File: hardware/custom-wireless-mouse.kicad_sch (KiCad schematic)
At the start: 31 parts, among them J1 SWD_HEADER, SW1 JS202011SCQN, SW2 EVQ-P7B01P, SW3 EVQ-P7B01P, SW4 EVQ-P7B01P, U1 nRF52810-QCAA-T, U2 PMW3610DM-SUDU, U3 TLV61220DBVT, Y1 NX2016SA-32MHZ

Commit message: Manual schematic cleanup pass (layout, routing, net naming)
Reworked wire routing and component placement by hand for readability,
and renamed several nets (VBAT/VBAT_SW, nRESET, etc). Known issues from
an audit of this pass, not yet fixed:

- J1's physical pin assignment no longer matches its own symbol's pin
  labels: pin 1 (labeled SWDIO) now carries nRESET, pin 3 (labeled GND)
  carries SWDIO, pin 4 (labeled ~RESET) carries GND. Only pin 2 (SWDCLK)
  is still correct.
- 5 of the 6 PWR_FLAG markers were removed, so ERC now flags U2's
  charge-pump/laser-driver nets, U3's VBAT net, and the GND net as
  undriven. Wiring on all of these is still correct per the netlist;
  this is only a missing ERC marker, not a wrong connection.
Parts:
- B1: value 1x AA (reused from kit) -> 1x AA
- C14: value 100nF X7R -> 100nF
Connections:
- net +VSYS: now also C1.1, C10.1, C11.1, C16.1, C2.1, C3.1, C4.1, C5.1, C8.1, C9.1, U1.1 (DEC1), U1.21 (DEC2), U1.22 (DEC3), U1.30 (DEC4); no longer C10.2, C11.2, C16.2, C5.2, C8.2, C9.2, L1.1, L1.2, U3.1 (SW)
- net GND: now also C1.2, C10.2, C11.2, C12.2, C13.2, C15.2, C16.2, C2.2, C3.2, C4.2, C5.2, C8.2, C9.2, J1.4 (~RESET); no longer C1.1, C10.1, C11.1, C12.1, C13.1, C15.1, C16.1, C2.1, C3.1, C4.1, C5.1, C8.1, C9.1, J1.3 (GND)
- net SWDIO: now reaches U1.18 (SWDIO)
- net SWDIO: now also J1.3 (GND); no longer J1.1 (SWDIO)
- net SWDCLK: now reaches J1.2 (SWDCLK), U1.17 (SWDCLK)
- net nRESET: now reaches U1.16 (P0.21/~{RESET})
- net nRESET: now also J1.1 (SWDIO); no longer J1.4 (~RESET)
- net VBAT_SW: now reaches SW1.1 (1A), U3.3 (EN), U3.6 (VBAT)
- net VBAT_SW: now also C15.1, L1.1; no longer B1.1 (+), C15.2, SW1.2 (2A)
- net at C6.2, U1.23 (XC1), Y1.3: no longer C7.1, U1.24 (XC2), Y1.1
- new net: B1.1 (+), SW1.2 (2A)
- new net: C12.1, C13.1, U2.9 (VCP)
- new net: U2.15 (XYLASER), U2.16 (-VCSEL)
- new net: L1.2, U3.1 (SW)
- new net: C7.1, U1.24 (XC2), Y1.1
- no-connect marks 7 -> 10
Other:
- note added: "MCU - U1 (nRF52810)"
- note removed: "MCU — U1 (nRF52810)"
- moved on the sheet: B1, C1, C10, C11, C12, C13, C15, C16, C2, C3, C4, C5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

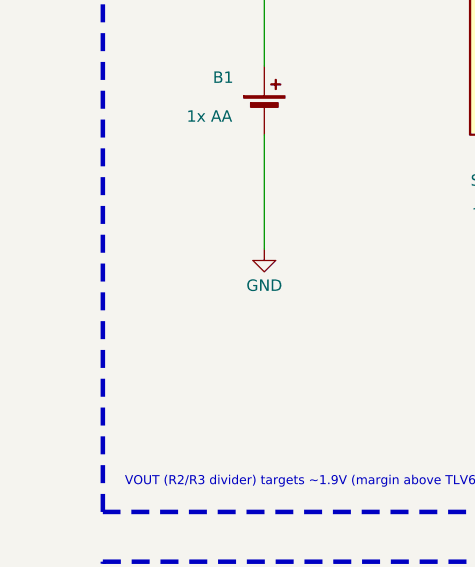
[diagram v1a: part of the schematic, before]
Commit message: Add JST B2B-XH-A battery connector to schematic and libraries
B1 (Device:Battery_Cell) is netted in the schematic but has an empty
Footprint field, so nothing would be placed on the PCB for it - there
was no physical way to actually plug in a battery. Added the JST XH
2-position pin header (B2B-XH-A) as J2, vendored from KiCad's own
official Connector_JST library (symbol, footprint, and 3D model, all
CC-BY-SA 4.0) plus its public datasheet. Placed unwired on the
schematic for manual wiring.
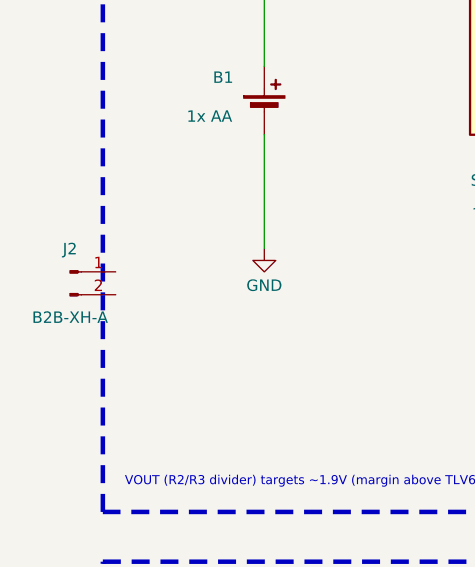
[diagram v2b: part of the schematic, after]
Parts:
- added J2: B2B-XH-A, jst-b2b-xh-a:battery-conn-jst-b2b-xh-a, symbol jst-b2b-xh-a:B2B-XH-A
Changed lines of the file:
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@@
+	)
+	(symbol
+		(lib_id "jst-b2b-xh-a:B2B-XH-A")
+		(at 12.7 90.17 0)
+		(unit 1)
+		(body_style 1)
+		(exclude_from_sim no)
+		(in_bom yes)
+		(on_board yes)
+		(in_pos_files yes)
+		(dnp no)
+		(property "Reference" "J2"
+			(at 12.7 87.63 0)
+			(show_name no)
+			(do_not_autoplace no)
+			(effects
+				(font
+					(size 1.27 1.27)
+				)
+			)
+		)
+		(property "Value" "B2B-XH-A"
+			(at 12.7 95.25 0)
+			(show_name no)
+			(do_not_autoplace no)
+			(effects
+				(font
+					(size 1.27 1.27)
+				)
+			)
+		)
+		(property "Footprint" "jst-b2b-xh-a:battery-conn-jst-b2b-xh-a"
+			(at 12.7 90.17 0)
+			(hide yes)
+			(show_name no)
+			(do_not_autoplace no)
+			(effects
+				(font
+					(size 1.27 1.27)
+				)
+			)
+		)
+		(property "Datasheet" "${KIPRJMOD}/datasheets/jst-xh-connector-series.pdf"
+			(at 12.7 90.17 0)
+			(hide yes)
+			(show_name no)
+			(do_not_autoplace no)
+			(effects
+				(font
+					(size 1.27 1.27)
+				)
+			)
+		)
+		(property "Description" "JST XH series 2.50mm-pitch battery connector, through-hole vertical pin header (mates with JST XHP-2 wire housing)"
+			(at 12.7 90.17 0)
+			(hide yes)
+			(show_name no)
+			(do_not_autoplace no)
+			(effects
+				(font
+					(size 1.27 1.27)
+				)
+			)
+		)
+		(pin "1"
+		)
+		(pin "2"
+		)
+		(instances
+			(project "custom-wireless-mouse"
+				(path "/d776ca83-3842-4947-ae63-5f40f232181f"
+					(reference "J2")
+					(unit 1)
+				)
+			)
+		)
 	)
 	(symbol

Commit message: Add reverse-battery and short-circuit protection parts (unwired)
Placed Q1 (Diodes Inc DMP2035U, low-threshold P-channel MOSFET) and F1
(Littelfuse 0603L010 PPTC resettable fuse) on the schematic near J2,
vendored with real datasheets. Q1 is a high-side ideal-diode reverse-
polarity protector (Source toward the battery, Drain toward the rest
of the circuit, Gate to GND); F1 is a self-resetting fuse sized well
above the design's peak draw but well below a battery short. Both
parts are placed only - not wired in - per request.

Also includes the removal of the old placeholder B1 (Device:Battery_Cell)
and repositioning of J2, done directly in the KiCad GUI.
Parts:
- removed B1: 1x AA, symbol Device:Battery_Cell
- added F1: 0603L010, littelfuse-0603l010:fuse-0603-littelfuse-0603l010, symbol littelfuse-0603l010:0603L010
- added Q1: DMP2035U, diodes-dmp2035u:sot-23-dmp2035u, symbol diodes-dmp2035u:DMP2035U
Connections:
- net GND: now also J2.2 (-)
- net at SW1.2 (2A): now also J2.1 (+)
- net FB: now reaches R2.2, R3.1, U3.4 (FB)
- net SW: now reaches L1.2, U3.1 (SW)
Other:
- note added: "MCU : U1 (nRF52810)"
- note added: "OPTICAL SENSOR : U2 (PMW3610)"
- note added: "POWER SUPPLY : U3 (TLV61220)"
- note added: "USER INPUT : WHEEL & BUTTONS"
- note removed: "MCU - U1 (nRF52810)"
- note removed: "OPTICAL SENSOR — U2 (PMW3610)"
- note removed: "POWER SUPPLY"
- note removed: "USER INPUT — WHEEL & BUTTONS"
- company: (none) -> Limp Dawg Customs
- moved on the sheet: J2

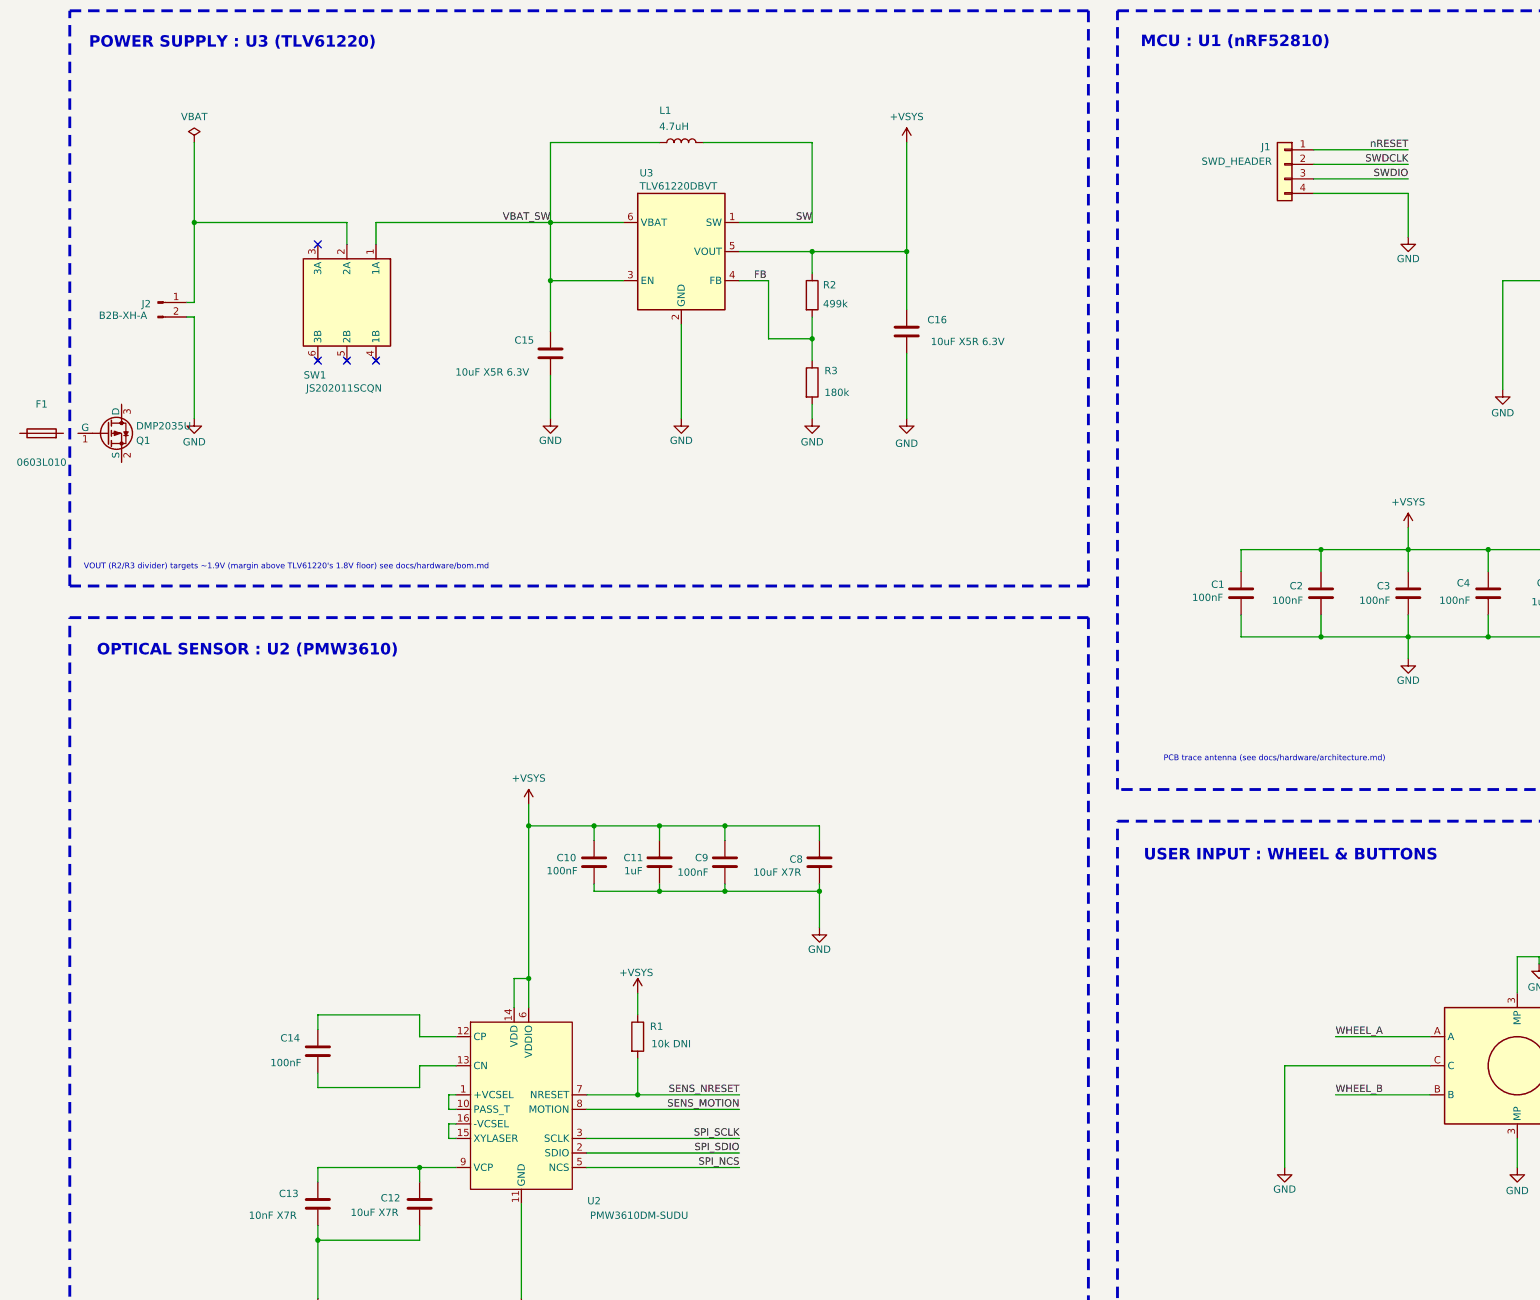
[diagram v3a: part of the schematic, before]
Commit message: Fix remaining ERC errors with PWR_FLAG markers, no rewiring
Added 7 local:PWR_FLAG instances (no existing parts moved) to satisfy
ERC's power_pin_not_driven / pin_not_driven checks:

- U2 (PMW3610) CP, CN, VCP, PASS_T/+VCSEL, and XYLASER/-VCSEL nets -
  all internally driven by the sensor's own charge pump, which ERC
  can't see, so each needs its own flag.
- U3's VBAT_SW net, undriven since Q1 (a passive-type MOSFET pin) sits
  between the battery and the regulator instead of a power-type source.
- The rotary encoder's local ground net (previously #PWR006), which
  was disconnected from the main GND driver.

ERC now reports 0 errors. The 2 remaining warnings are not fixable
this way: ENC1's lib_symbol_mismatch is a cosmetic KiCad comparison
quirk (the cached copy is byte-identical to the library file), and the
ANT isolated-pin-label warning is expected for a single-ended antenna
trace net.
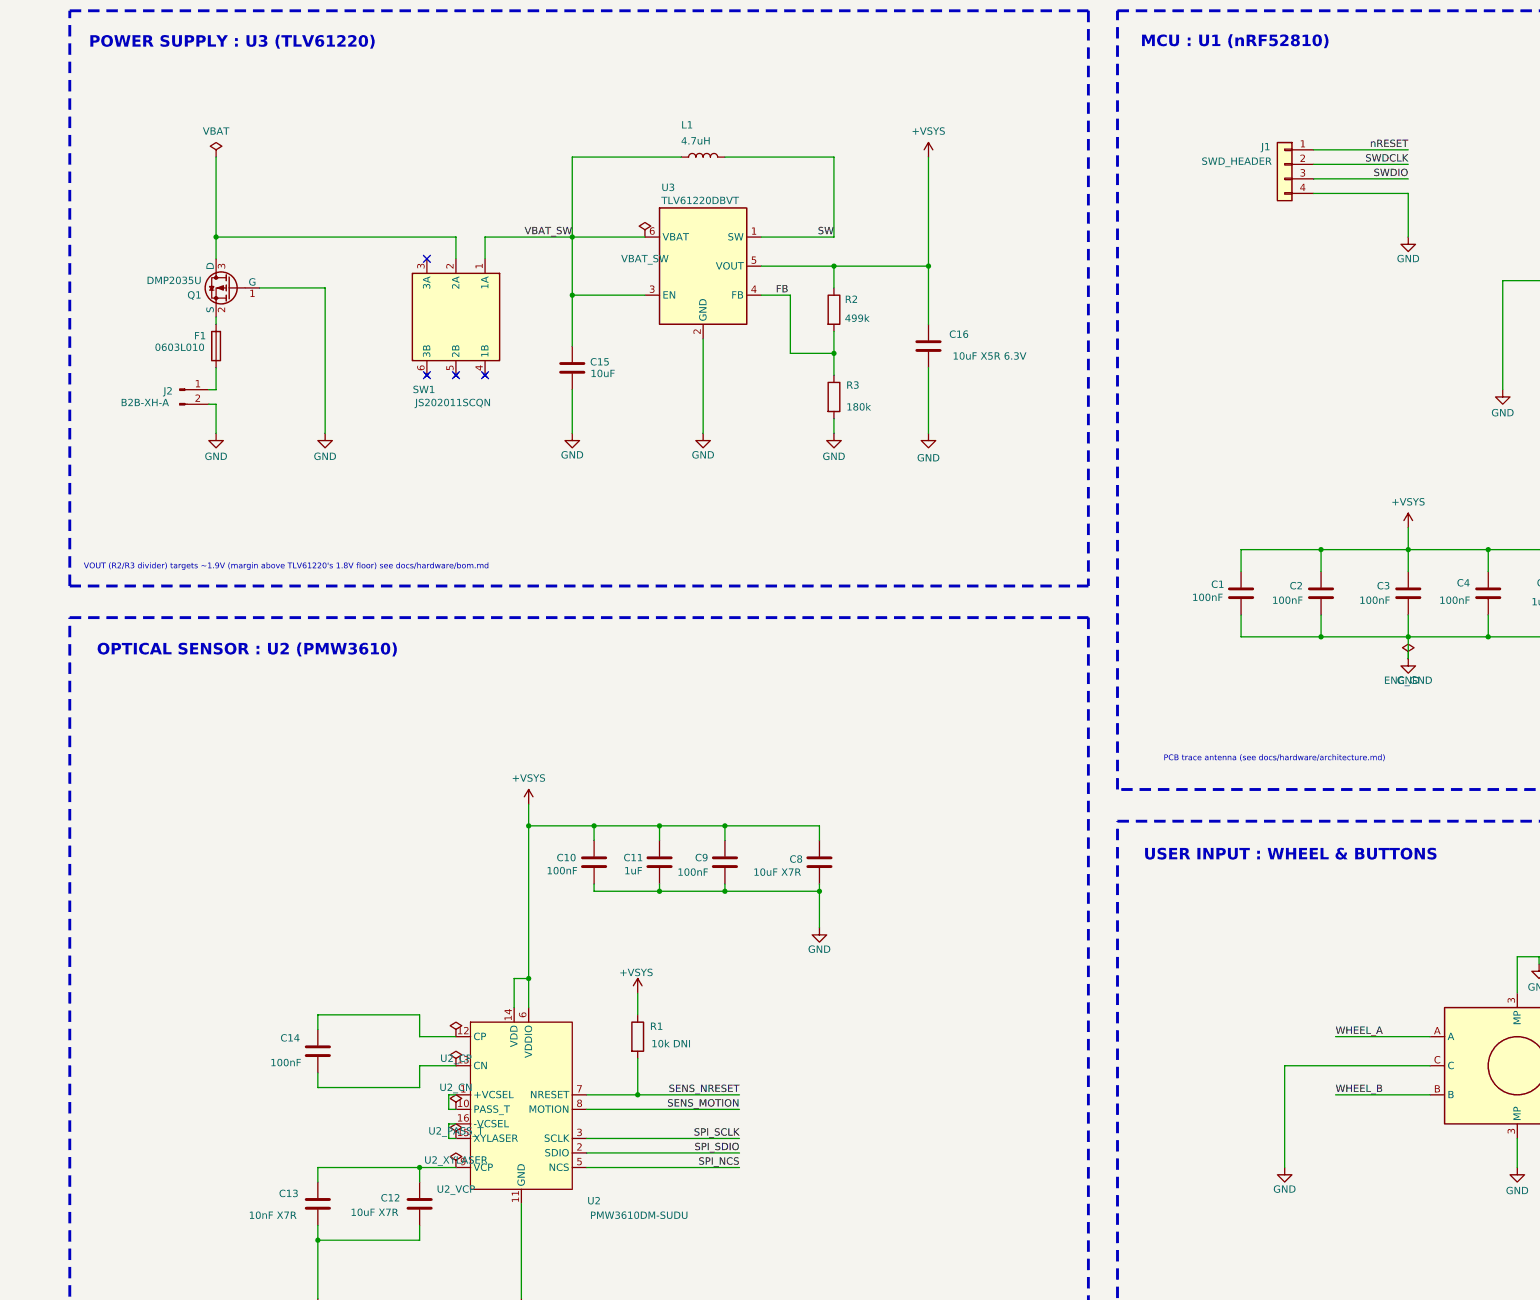
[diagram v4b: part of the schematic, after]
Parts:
- C15: value 10uF X5R 6.3V -> 10uF
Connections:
- net GND: now also Q1.1 (G)
- net at F1.1: now also J2.1 (+)
- net at F1.2: now also Q1.2 (S)
- net at Q1.3 (D): now also SW1.2 (2A)
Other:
- moved on the sheet: C15, C16, F1, J2, L1, Q1, R2, R3, SW1, U3

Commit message: Minor GUI cleanup pass on top of the new protection/PWR_FLAG additions
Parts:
- C16: value 10uF X5R 6.3V -> 10uF
